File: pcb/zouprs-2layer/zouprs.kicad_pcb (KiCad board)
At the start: 2 copper layers, 9 parts, among them J1 Conn_Coaxial

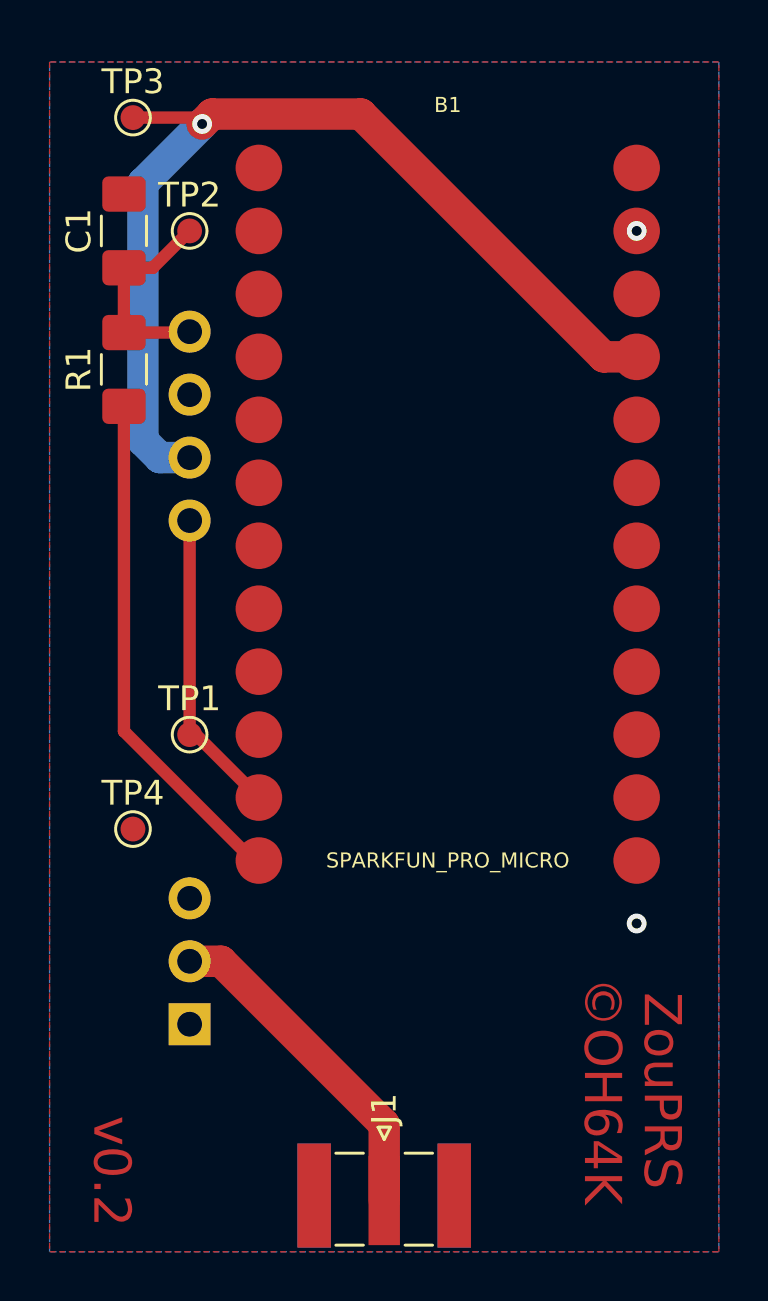
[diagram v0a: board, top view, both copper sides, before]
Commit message: Move Arduino board about 1mm up
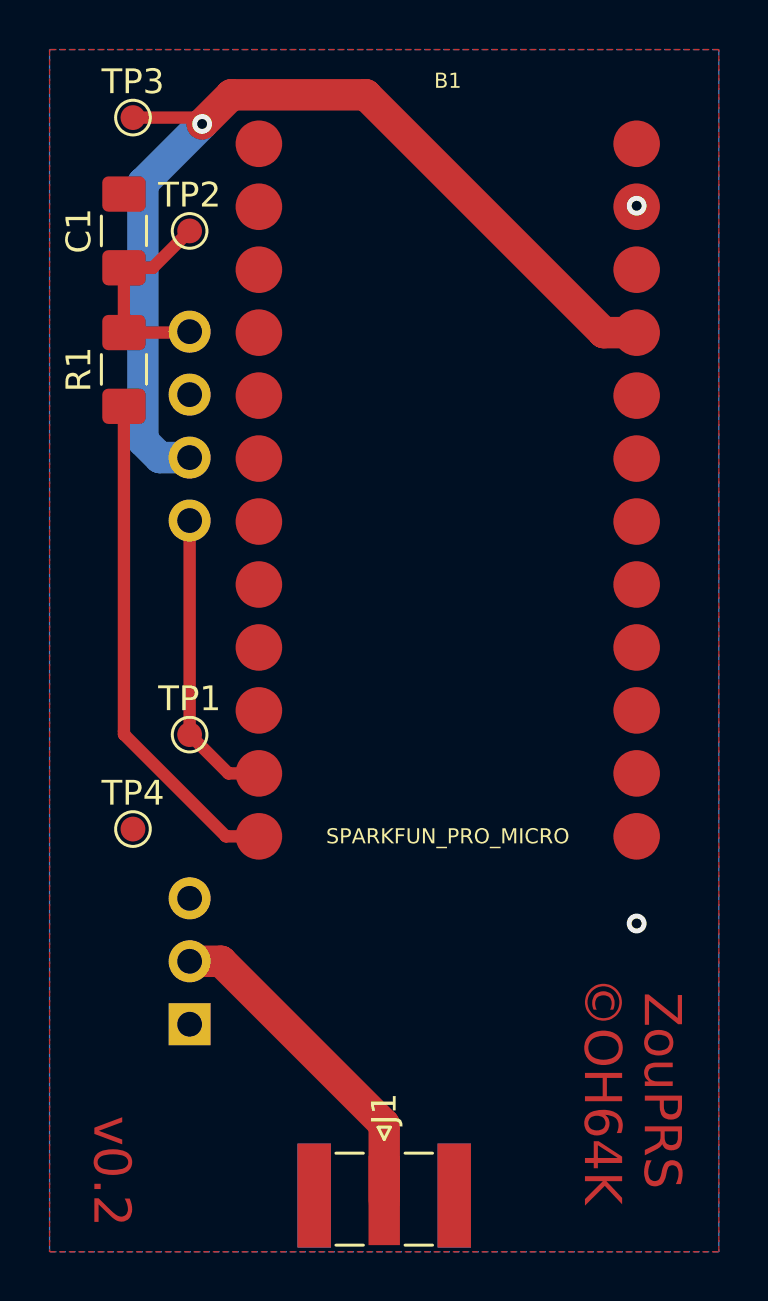
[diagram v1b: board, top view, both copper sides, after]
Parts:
- moved B1 0.98 mm to (131.1, 61.0)
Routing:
- net EN: track 12.3 -> 11.8 mm

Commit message: Add some ground vias to RF end of the board
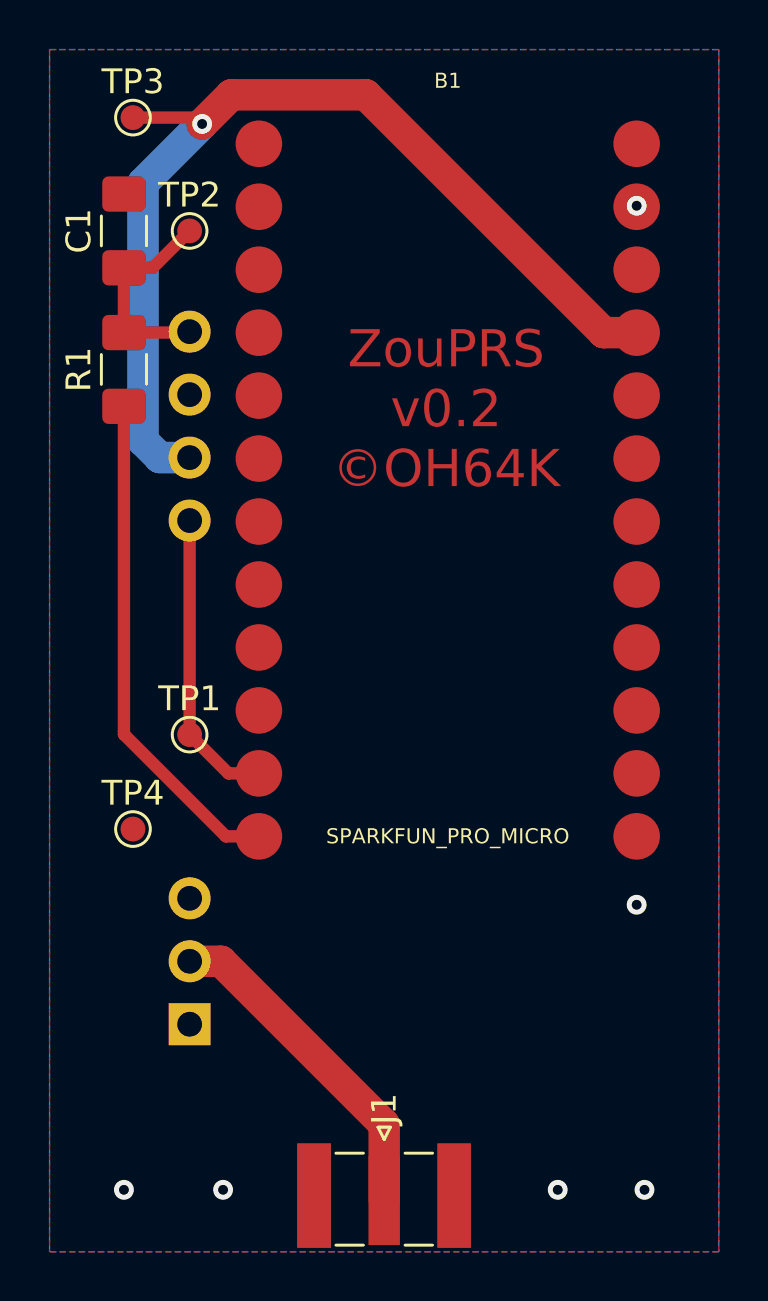
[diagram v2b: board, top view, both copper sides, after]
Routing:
- net GND: vias 2 -> 6
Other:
- board text added: "ZouPRS v0.2 ©OH64K"
- board text removed: "ZouPRS ©OH64K"
- board text removed: "v0.2"
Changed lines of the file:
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@@
   (general
     (thickness 1.6)
-    (drawings 2)
-    (tracks 30)
+    (drawings 1)
+    (tracks 34)
     (zones 0)
     (modules 9)
@@
     )
   )
-  (gr_text v0.2 (at 117.5 92 270) (layer F.Cu)
-    (effects (font (size 1.5 1.5) (thickness 0.3)) (justify right))
-  )
-  (gr_text "ZouPRS\n©OH64K" (at 138.5 86.5 270) (layer F.Cu)
+  (gr_text "ZouPRS\nv0.2\n©OH64K" (at 131 59) (layer F.Cu)
     (effects (font (size 1.5 1.5) (thickness 0.3)))
   )
-  (via (at 138.684 79.756) (size 0.8) (drill 0.4) (layers F.Cu B.Cu) (net 2))
+  (via (at 138.684 79) (size 0.8) (drill 0.4) (layers F.Cu B.Cu) (net 2))
   (via (at 138.684 50.8) (size 0.8) (drill 0.4) (layers F.Cu B.Cu) (net 2))
+  (via (at 118 90.5) (size 0.8) (drill 0.4) (layers F.Cu B.Cu) (net 2))
+  (via (at 139 90.5) (size 0.8) (drill 0.4) (layers F.Cu B.Cu) (net 2))
+  (via (at 135.5 90.5) (size 0.8) (drill 0.4) (layers F.Cu B.Cu) (net 2))
+  (via (at 122 90.5) (size 0.8) (drill 0.4) (layers F.Cu B.Cu) (net 2))
   (segment (start 119.1625 53.3035) (end 120.65 51.816) (width 0.5) (layer F.Cu) (net 20))
   (segment (start 118 53.3035) (end 119.1625 53.3035) (width 0.5) (layer F.Cu) (net 20))

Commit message: Small tweaks to test point
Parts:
- moved TP3 0.45 mm to (118.0, 47.5)
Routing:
- net +5V: track 40.8 -> 41.4 mm
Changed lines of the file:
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@@
     (thickness 1.6)
     (drawings 1)
-    (tracks 34)
+    (tracks 35)
     (zones 0)
     (modules 9)
@@
   )
   (module TestPoint:TestPoint_Pad_D1.0mm (layer F.Cu)
-    (at 118.364 47.244)
+    (at 118 47.5)
     (descr "SMD pad as test Point, diameter 1.0mm")
     (tags "test point SMD pad")
@@
   (segment (start 120.65 60.96) (end 119.447919 60.96) (width 1.27) (layer B.Cu) (net 23))
   (segment (start 120.897602 47.244) (end 121.154801 47.501199) (width 0.5) (layer F.Cu) (net 23))
-  (segment (start 118.364 47.244) (end 120.897602 47.244) (width 0.5) (layer F.Cu) (net 23))
   (segment (start 127.760122 46.325199) (end 137.354923 55.92) (width 1.27) (layer F.Cu) (net 23))
   (segment (start 137.354923 55.92) (end 138.684 55.92) (width 1.27) (layer F.Cu) (net 23))
   (segment (start 122.330801 46.325199) (end 127.760122 46.325199) (width 1.27) (layer F.Cu) (net 23))
   (segment (start 121.154801 47.501199) (end 122.330801 46.325199) (width 1.27) (layer F.Cu) (net 23))
+  (segment (start 118.001199 47.501199) (end 118 47.5) (width 0.5) (layer F.Cu) (net 23))
+  (segment (start 121.154801 47.501199) (end 118.001199 47.501199) (width 0.5) (layer F.Cu) (net 23))
   (segment (start 128.5 87.862) (end 128.5 90.932) (width 1.27) (layer F.Cu) (net 24))
   (segment (start 121.918 81.28) (end 128.5 87.862) (width 1.27) (layer F.Cu) (net 24))
